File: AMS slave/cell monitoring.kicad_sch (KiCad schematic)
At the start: 74 parts, among them J1 529010274, Q1 KY2N7002, SW1 SW_Push, U1 BQ76940DBT

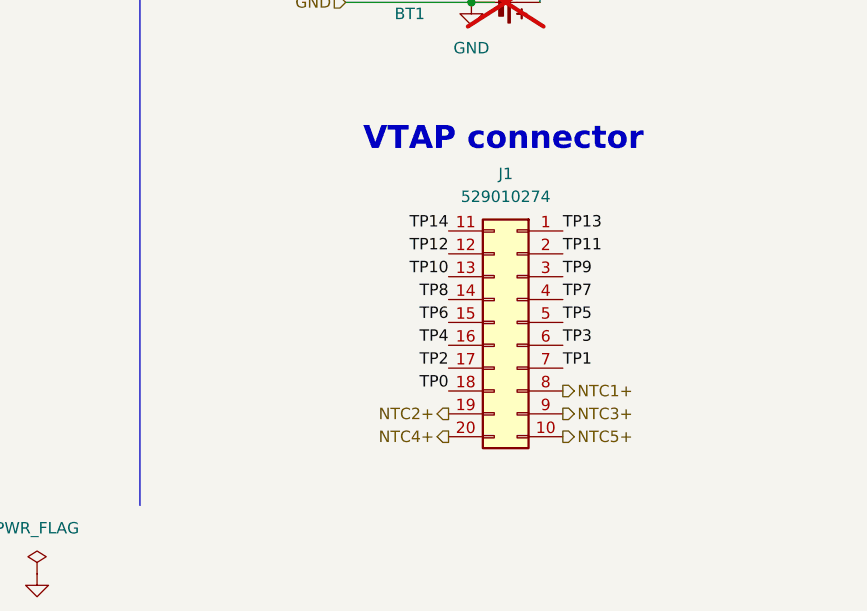
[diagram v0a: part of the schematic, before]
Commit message: fixed VTAP collisions, AMS slave redesign WIP
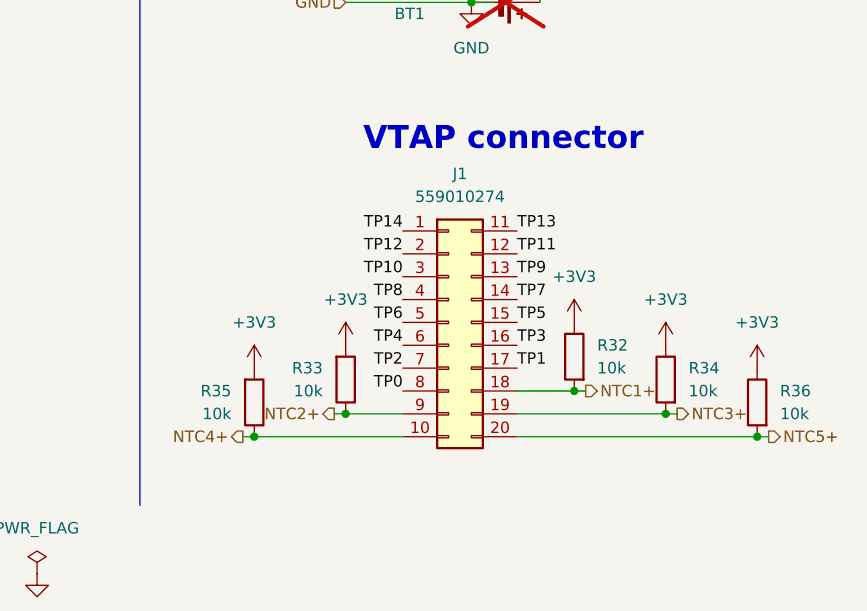
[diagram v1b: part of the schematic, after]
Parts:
- added R32, R33, R34, R35, R36: 10k, RMC_Resistor:R_0805_2012Metric_Pad1.20x1.40mm_HandSolder_L, symbol Device:R
- J1: value 529010274 -> 559010274; footprint (none) -> CON_550910274_MOL:CON_550910274_MOL
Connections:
- net +3V3: now also R32.1, R33.2, R34.1, R35.2, R36.1
- net GND: now also J1.8 (Pin_8); no longer J1.18 (Pin_18)
- net NTC1+: now also J1.18 (Pin_18), R32.2; no longer J1.8 (Pin_8)
- net NTC2+: now also J1.9 (Pin_9), R33.1; no longer J1.19 (Pin_19)
- net NTC3+: now also J1.19 (Pin_19), R34.2; no longer J1.9 (Pin_9)
- net NTC4+: now also J1.10 (Pin_10), R35.1; no longer J1.20 (Pin_20)
- net NTC5+: now also J1.20 (Pin_20), R36.2; no longer J1.10 (Pin_10)
- net PACK+: now also J1.1 (Pin_1); no longer J1.11 (Pin_11)
- net TP1: now also J1.17 (Pin_17); no longer J1.7 (Pin_7)
- net TP10: now also J1.3 (Pin_3); no longer J1.13 (Pin_13)
- net TP11: now also J1.12 (Pin_12); no longer J1.2 (Pin_2)
- net TP12: now also J1.2 (Pin_2); no longer J1.12 (Pin_12)
- net TP13: now also J1.11 (Pin_11); no longer J1.1 (Pin_1)
- net TP2: now also J1.7 (Pin_7); no longer J1.17 (Pin_17)
- net TP3: now also J1.16 (Pin_16); no longer J1.6 (Pin_6)
- net TP4: now also J1.6 (Pin_6); no longer J1.16 (Pin_16)
- net TP5: now also J1.15 (Pin_15); no longer J1.5 (Pin_5)
- net TP6: now also J1.5 (Pin_5); no longer J1.15 (Pin_15)
- net TP7: now also J1.14 (Pin_14); no longer J1.4 (Pin_4)
- net TP8: now also J1.4 (Pin_4); no longer J1.14 (Pin_14)
- net TP9: now also J1.13 (Pin_13); no longer J1.3 (Pin_3)
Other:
- moved on the sheet: J1

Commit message: AMS slave WIP
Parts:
- J1: symbol Connector_Generic:Conn_02x10_Top_Bottom -> Connector_Generic_MountingPin:Conn_02x10_Top_Bottom_MountingPin
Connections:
- no-connect marks 2 -> 3
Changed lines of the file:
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@@
 	)
 	(no_connect
+		(at 241.3 162.56)
+	)
+	(no_connect
 		(at 50.8 92.71)
 	)
@@
 	)
 	(symbol
-		(lib_id "Connector_Generic:Conn_02x10_Top_Bottom")
+		(lib_id "Connector_Generic_MountingPin:Conn_02x10_Top_Bottom_MountingPin")
 		(at 240.03 144.78 0)
 		(unit 1)
@@
 			)
 		)
-		(property "Description" "Generic connector, double row, 02x10, top/bottom pin numbering scheme (row 1: 1...pins_per_row, row2: pins_per_row+1 ... num_pins), script generated (kicad-library-utils/schlib/autogen/connector/)"
+		(property "Description" "Generic connectable mounting pin connector, double row, 02x10, top/bottom pin numbering scheme (row 1: 1...pins_per_row, row2: pins_per_row+1 ... num_pins), script generated (kicad-library-utils/schlib/autogen/connector/)"
 			(at 240.03 144.78 0)
 			(effects
@@
 		(pin "19"
 		)
+		(pin "MP"
+		)
 		(instances

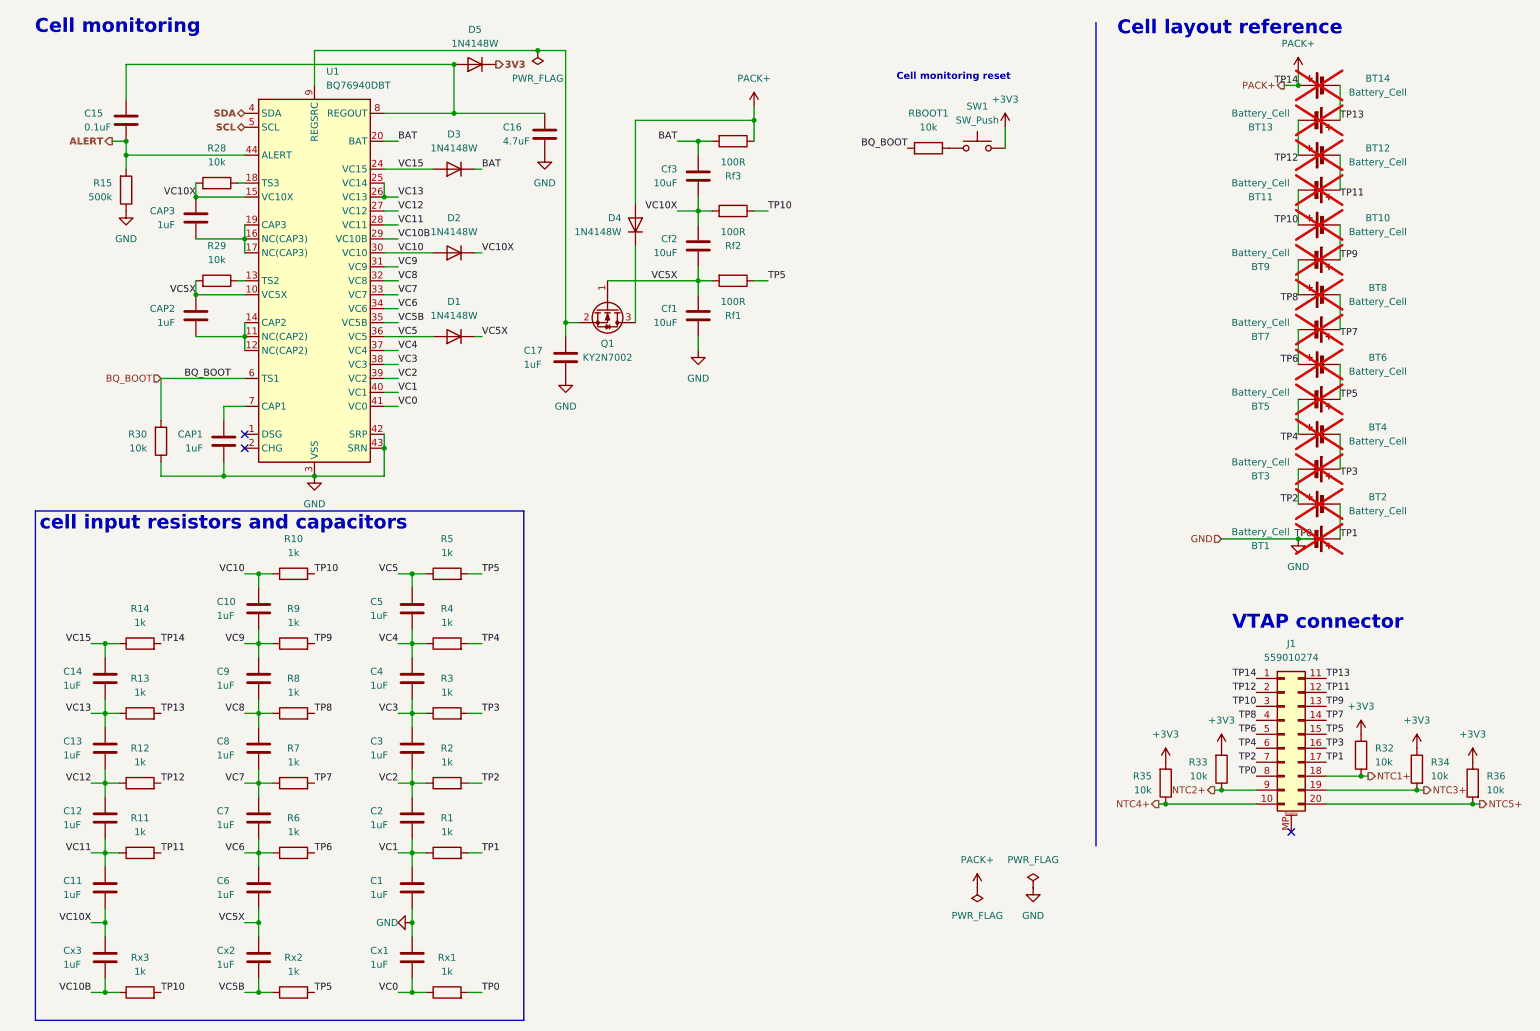
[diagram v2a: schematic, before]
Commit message: AMS slave schem updated
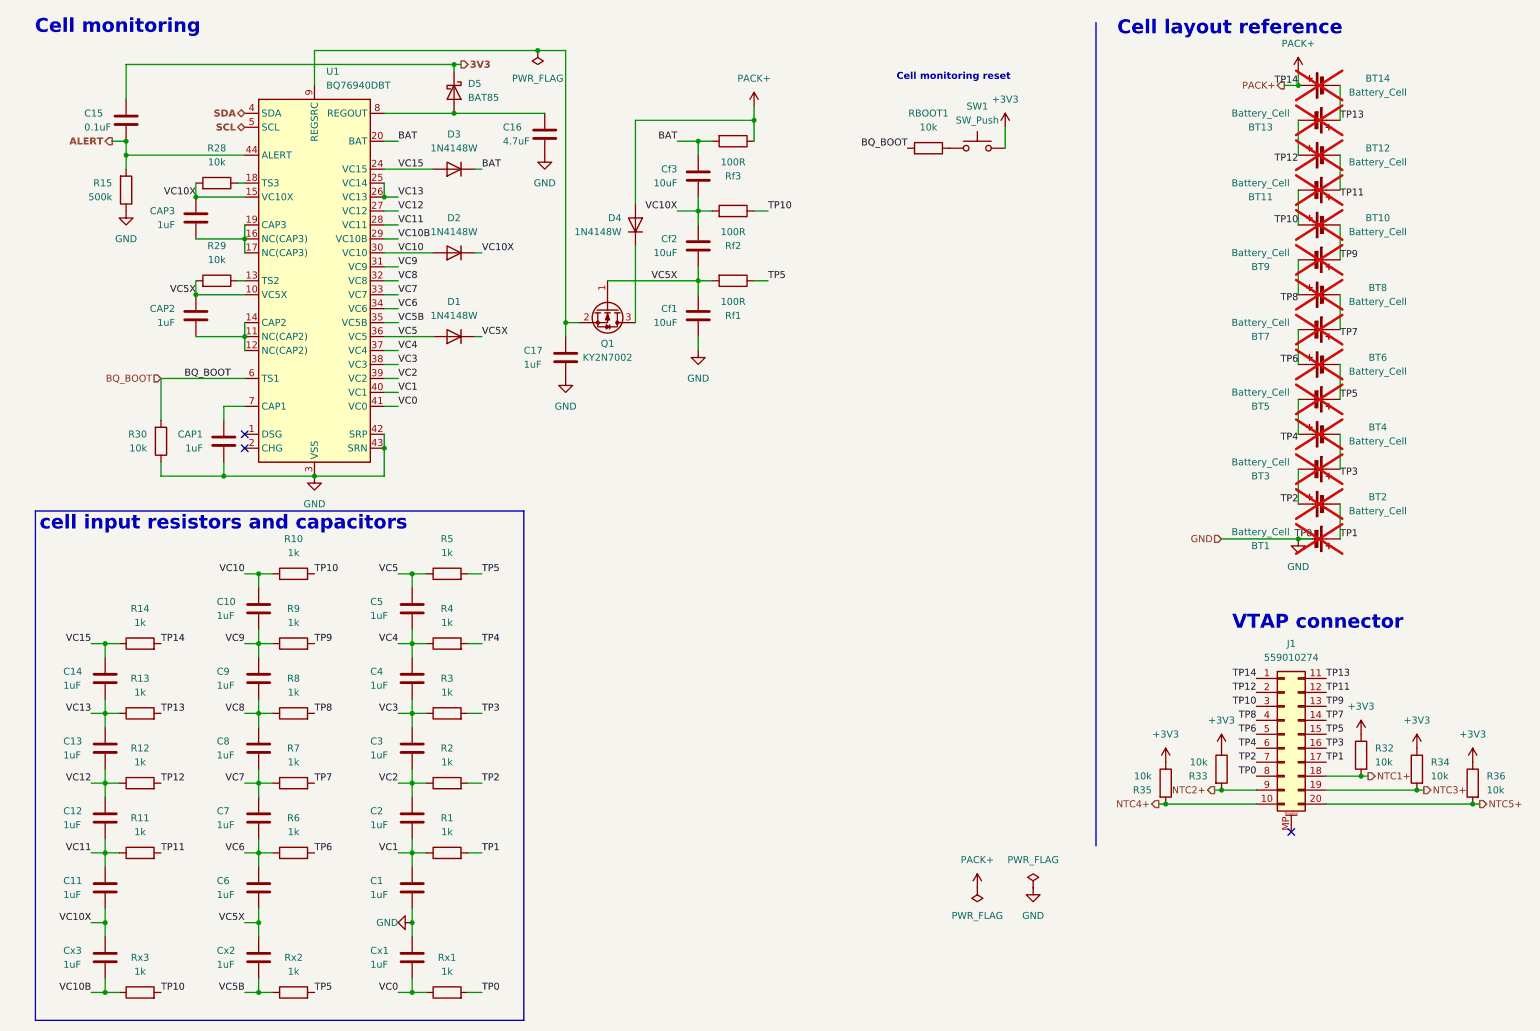
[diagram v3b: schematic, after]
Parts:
- removed D5: 1N4148W, Diode_SMD:D_0805_2012Metric_Pad1.15x1.40mm_HandSolder, symbol Device:D
- added D5: BAT85, Diode_THT:D_DO-35_SOD27_P7.62mm_Horizontal, symbol Diode:BAT85
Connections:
- net +3V3: now also R33.1, R35.1; no longer R33.2, R35.2
- net 3V3: now also C15.2, D5.1 (K)
- net NTC2+: now also R33.2; no longer R33.1
- net NTC4+: now also R35.2; no longer R35.1
- net at C16.2, U1.8 (REGOUT): now also D5.2 (A); no longer C15.2
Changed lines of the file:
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@@
 	)
 	(junction
-		(at 228.6 154.94)
-		(diameter 0)
-		(color 0 0 0 0)
-	)
-	(junction
 		(at 50.8 72.39)
 		(diameter 0)
@@
 	)
 	(junction
-		(at 88.9 22.86)
-		(diameter 0)
-		(color 0 0 0 0)
-	)
-	(junction
 		(at 41.91 46.99)
 		(diameter 0)
@@
 	)
 	(junction
-		(at 25.4 191.77)
+		(at 218.44 157.48)
 		(diameter 0)
 		(color 0 0 0 0)
 	)
 	(junction
-		(at 88.9 31.75)
+		(at 25.4 191.77)
 		(diameter 0)
 		(color 0 0 0 0)
@@
 	)
 	(junction
-		(at 218.44 157.48)
-		(diameter 0)
-		(color 0 0 0 0)
-	)
-	(junction
 		(at 25.4 166.37)
 		(diameter 0)
@@
 	)
 	(junction
+		(at 228.6 154.94)
+		(diameter 0)
+		(color 0 0 0 0)
+	)
+	(junction
 		(at 25.4 128.27)
 		(diameter 0)
@@
 	)
 	(junction
+		(at 88.9 22.86)
+		(diameter 0)
+		(color 0 0 0 0)
+	)
+	(junction
+		(at 88.9 31.75)
+		(diameter 0)
+		(color 0 0 0 0)
+	)
+	(junction
 		(at 81.28 153.67)
 		(diameter 0)
@@
 	(wire
 		(pts
-			(xy 228.6 154.94) (xy 234.95 154.94)
-		)
-		(stroke
-			(width 0)
-			(type default)
-		)
-	)
-	(wire
-		(pts
 			(xy 25.4 191.77) (xy 25.4 189.23)
 		)
@@
 	(wire
 		(pts
+			(xy 76.2 31.75) (xy 88.9 31.75)
+		)
+		(stroke
+			(width 0)
+			(type default)
+		)
+	)
+	(wire
+		(pts
 			(xy 116.84 62.23) (xy 133.35 62.23)
 		)
@@
 	(wire
 		(pts
-			(xy 218.44 157.48) (xy 234.95 157.48)
-		)
-		(stroke
-			(width 0)
-			(type default)
-		)
-	)
-	(wire
-		(pts
 			(xy 25.4 128.27) (xy 25.4 130.81)
 		)
@@
 		)
 	)
-	(wire
-		(pts
-			(xy 88.9 22.86) (xy 88.9 31.75)
-		)
-		(stroke
-			(width 0)
-			(type default)
-		)
-	)
 	(polyline
 		(pts
@@
 	(wire
 		(pts
-			(xy 76.2 31.75) (xy 88.9 31.75)
-		)
-		(stroke
-			(width 0)
-			(type default)
-		)
-	)
-	(wire
-		(pts
 			(xy 50.8 52.07) (xy 50.8 54.61)
 		)
@@
 	(wire
 		(pts
+			(xy 228.6 154.94) (xy 234.95 154.94)
+		)
+		(stroke
+			(width 0)
+			(type default)
+		)
+	)
+	(wire
+		(pts
 			(xy 78.74 140.97) (xy 81.28 140.97)
 		)
@@
 	(wire
 		(pts
+			(xy 88.9 22.86) (xy 88.9 24.13)
+		)
+		(stroke
+			(width 0)
+			(type default)
+		)
+	)
+	(wire
+		(pts
 			(xy 78.74 191.77) (xy 81.28 191.77)
 		)
@@
 	(wire
 		(pts
+			(xy 218.44 157.48) (xy 234.95 157.48)
+		)
+		(stroke
+			(width 0)
+			(type default)
+		)
+	)
+	(wire
+		(pts
 			(xy 46.99 85.09) (xy 50.8 85.09)
 		)
@@
 	(wire
 		(pts
+			(xy 88.9 22.86) (xy 90.17 22.86)
+		)
+		(stroke
+			(width 0)
+			(type default)
+		)
+	)
+	(wire
+		(pts
 			(xy 81.28 179.07) (xy 81.28 181.61)
 		)
@@
 	(wire
 		(pts
+			(xy 88.9 31.75) (xy 105.41 31.75)
+		)
+		(stroke
+			(width 0)
+			(type default)
+		)
+	)
+	(wire
+		(pts
 			(xy 25.4 140.97) (xy 27.94 140.97)
 		)
@@
 	(wire
 		(pts
-			(xy 88.9 31.75) (xy 105.41 31.75)
-		)
-		(stroke
-			(width 0)
-			(type default)
-		)
-	)
-	(wire
-		(pts
 			(xy 92.71 57.15) (xy 93.98 57.15)
 		)
@@
 	(hierarchical_label "3V3"
 		(shape output)
-		(at 96.52 22.86 0)
+		(at 90.17 22.86 0)
 		(effects
 			(font
@@
 	)
 	(symbol
+		(lib_id "Diode:BAT85")
+		(at 88.9 27.94 270)
+		(unit 1)
+		(exclude_from_sim no)
+		(in_bom yes)
+		(on_board yes)
+		(dnp no)
+		(fields_autoplaced yes)
+		(property "Reference" "D5"
+			(at 91.44 26.3524 90)
+			(effects
+				(font
+					(size 1.27 1.27)
+				)
+				(justify left)
+			)
+		)
+		(property "Value" "BAT85"
+			(at 91.44 28.8924 90)
+			(effects
+				(font
+					(size 1.27 1.27)
+				)
+				(justify left)
+			)
+		)
+		(property "Footprint" "Diode_THT:D_DO-35_SOD27_P7.62mm_Horizontal"
+			(at 84.455 27.94 0)
+			(effects
+				(font
+					(size 1.27 1.27)
+				)
+				(hide yes)
+			)
+		)
+		(property "Datasheet" "https://assets.nexperia.com/documents/data-sheet/BAT85.pdf"
+			(at 88.9 27.94 0)
+			(effects
+				(font
+					(size 1.27 1.27)
+				)
+				(hide yes)
+			)
+		)
+		(property "Description" "30V 0.2A Schottky barrier single diode, DO-35"
+			(at 88.9 27.94 0)
+			(effects
+				(font
+					(size 1.27 1.27)
+				)
+				(hide yes)
+			)
+		)
+		(pin "2"
+		)
+		(pin "1"
+		)
+		(instances
+			(project ""
+				(path "/9d086174-c3f9-4f2b-b5ac-a2d10e7f2013/72ba2d86-b5f1-4c9f-9e37-5b2b76178c75"
+					(reference "D5")
+					(unit 1)
+				)
+			)
+		)
+	)
+	(symbol
 		(lib_id "Device:R")
 		(at 29.21 45.72 0)
@@
 		(lib_id "Device:R")
 		(at 228.6 151.13 0)
-		(mirror x)
 		(unit 1)
 		(exclude_from_sim no)
@@
 		(dnp no)
 		(property "Reference" "R33"
-			(at 226.06 149.8599 0)
+			(at 226.06 152.4001 0)
 			(effects
 				(font
@@
 		)
 		(property "Value" "10k"
-			(at 226.06 152.3999 0)
+			(at 226.06 149.8601 0)
 			(effects
 				(font
@@
 	)
 	(symbol
-		(lib_id "Device:D")
-		(at 92.71 22.86 180)
-		(unit 1)
-		(exclude_from_sim no)
-		(in_bom yes)
-		(on_board yes)
-		(dnp no)
-		(property "Reference" "D5"
-			(at 92.71 16.51 0)
-			(effects
-				(font
-					(size 1.27 1.27)
-				)
-			)
-		)
-		(property "Value" "1N4148W"
-			(at 92.71 19.05 0)
-			(effects
-				(font
-					(size 1.27 1.27)
-				)
-			)
-		)
-		(property "Footprint" "Diode_SMD:D_0805_2012Metric_Pad1.15x1.40mm_HandSolder"
-			(at 92.71 22.86 0)
-			(effects
-				(font
-					(size 1.27 1.27)
-				)
-				(hide yes)
-			)
-		)
-		(property "Datasheet" "~"
-			(at 92.71 22.86 0)
-			(effects
-				(font
-					(size 1.27 1.27)
-				)
-				(hide yes)
-			)
-		)
-		(property "Description" "Diode"
-			(at 92.71 22.86 0)
-			(effects
-				(font
-					(size 1.27 1.27)
-				)
-				(hide yes)
-			)
-		)
-		(property "Sim.Device" "D"
-			(at 92.71 22.86 0)
-			(effects
-				(font
-					(size 1.27 1.27)
-				)
-				(hide yes)
-			)
-		)
-		(property "Sim.Pins" "1=K 2=A"
-			(at 92.71 22.86 0)
-			(effects
-				(font
-					(size 1.27 1.27)
-				)
-				(hide yes)
-			)
-		)
-		(pin "2"
-		)
-		(pin "1"
-		)
-		(instances
-			(project "AMS slave"
-				(path "/9d086174-c3f9-4f2b-b5ac-a2d10e7f2013/72ba2d86-b5f1-4c9f-9e37-5b2b76178c75"
-					(reference "D5")
-					(unit 1)
-				)
-			)
-		)
-	)
-	(symbol
 		(lib_id "Device:C")
 		(at 53.34 160.02 180)
@@
 		(lib_id "Device:R")
 		(at 218.44 153.67 0)
-		(mirror x)
 		(unit 1)
 		(exclude_from_sim no)
@@
 		(dnp no)
 		(property "Reference" "R35"
-			(at 215.9 152.3999 0)
+			(at 215.9 154.9401 0)
 			(effects
 				(font
@@
 		)
 		(property "Value" "10k"
-			(at 215.9 154.9399 0)
+			(at 215.9 152.4001 0)
 			(effects
 				(font

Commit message: AMS slave schem 0.5.0 pcb 0.6.0, VTAP silkscreen
AMS slave changed to account for architectural changes
Schematic changes:
- power is now provided mainly through the 5V CAN input with voltage isolation
- BQ76940 thermistors moved to mcu
PCB changes:
- board to board connector requires all components to be on top surface
VTAP changes:
Added silkscreen to indicate cell and pack polarity
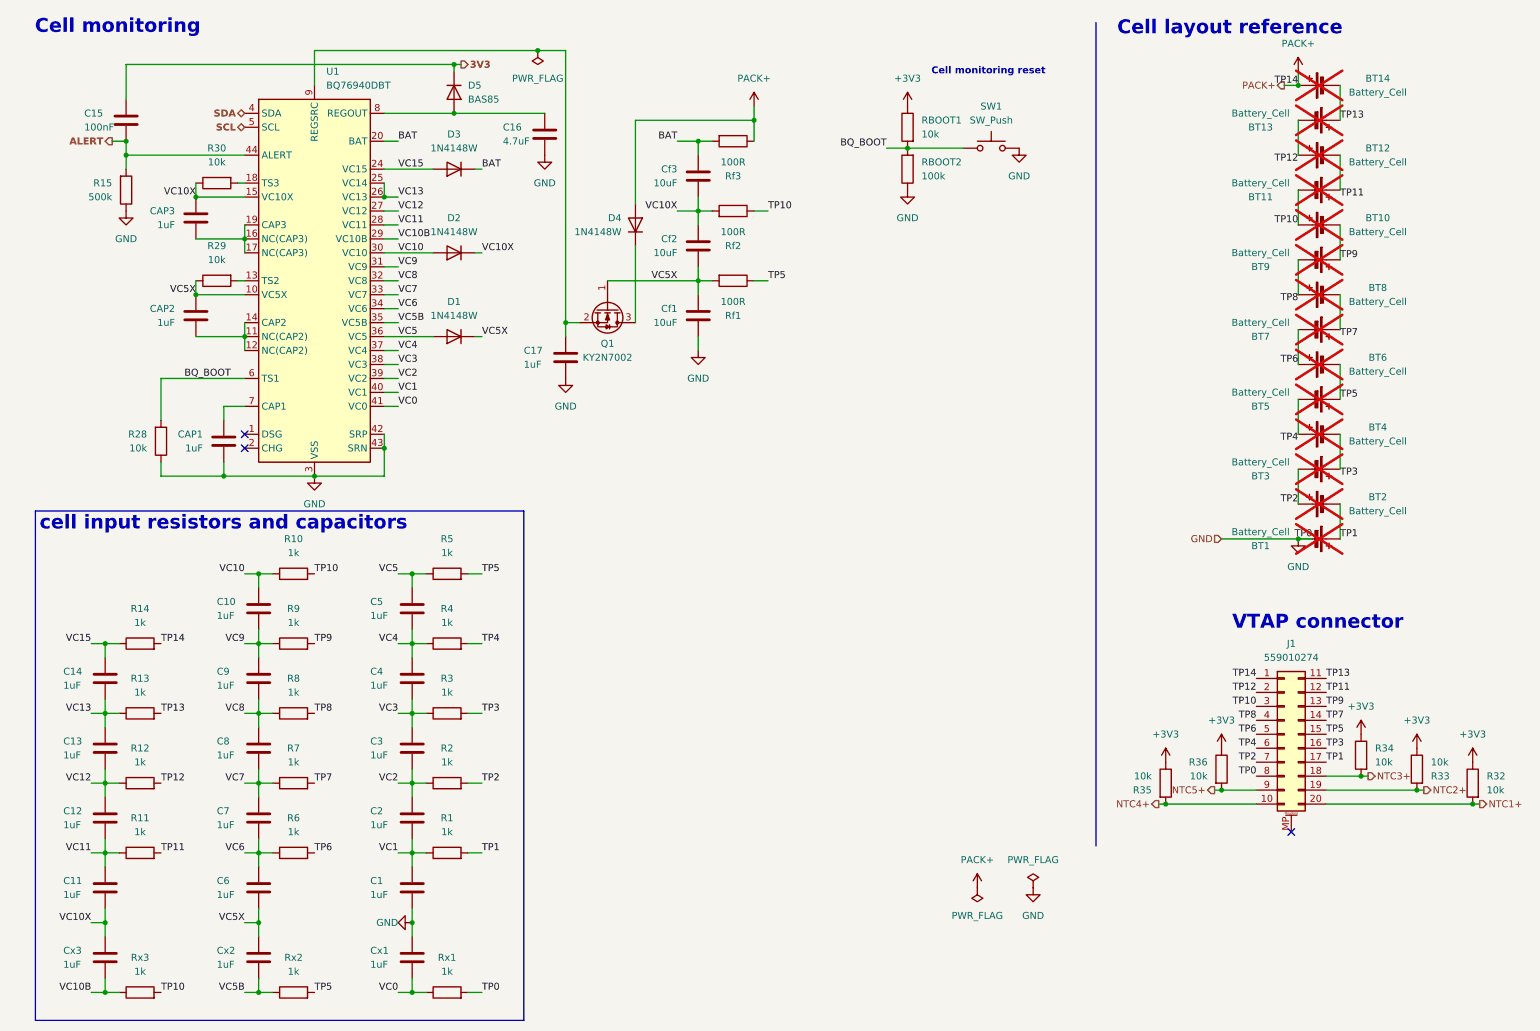
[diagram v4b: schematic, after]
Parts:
- removed D5: BAT85, Diode_THT:D_DO-35_SOD27_P7.62mm_Horizontal, symbol Diode:BAT85
- added D5: BAS85, Diode_SMD:D_MiniMELF, symbol Device:D
- added RBOOT2: 100k, RMC_Resistor:R_0805_2012Metric_Pad1.20x1.40mm_HandSolder_L, symbol Device:R
- C15: value 0.1uF -> 100nF
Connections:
- net +3V3: now also RBOOT1.1; no longer SW1.1
- net 3V3: now also D5.1 (K)
- net BQ_BOOT: now also R28.2, SW1.2, RBOOT2.2; no longer R30.2
- net GND: now also R28.1, SW1.1, RBOOT2.1; no longer R30.1
- net NTC1+: now also J1.20 (Pin_20); no longer J1.18 (Pin_18)
- net NTC2+: now also J1.19 (Pin_19); no longer J1.9 (Pin_9)
- net NTC3+: now also J1.18 (Pin_18); no longer J1.19 (Pin_19)
- net NTC5+: now also J1.9 (Pin_9); no longer J1.20 (Pin_20)
- net VC10X: now also R30.1; no longer R28.2
- net VC5X: now also R29.1; no longer R29.2
- net at C16.2, U1.8 (REGOUT): now also D5.2 (A)
- net at U1.18 (TS3): now also R30.2; no longer R28.1
- net at U1.13 (TS2): now also R29.2; no longer R29.1
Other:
- moved on the sheet: R28, R29, R30, R32, R33, R34, R36, RBOOT1, SW1
